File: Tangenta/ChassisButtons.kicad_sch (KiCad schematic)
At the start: 26 parts, among them J2 Conn_02x02_Top_Bottom, Q1 2N7002, Q2 2N7002, SW1 TSC015A04818B, SW2 TSC015A04818B, U7 74HC04D,653, U8 CD4060SA_TR, U9 74HC74D,653

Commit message: Fixes, new approach.
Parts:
- C34, C35, C36, C37, C38, C39: symbol LocalPrjLib:C_Small -> LocalSymbolsPrjLib:C_Small
- J2: symbol LocalPrjLib:Conn_02x02_Top_Bottom -> LocalSymbolsPrjLib:Conn_02x02_Top_Bottom
- Q1, Q2: symbol LocalPrjLib:2N7002 -> LocalSymbolsPrjLib:2N7002
- R15, R16, R17, R18, R19, R20, R21, R22, R23, R24, R25, R26: symbol LocalPrjLib:R_Small_US -> LocalSymbolsPrjLib:R_Small_US
- SW1, SW2: symbol LocalPrjLib:TSC015A04818B -> LocalSymbolsPrjLib:TSC015A04818B
- U7: symbol LocalPrjLib:74HC04D,653 -> LocalSymbolsPrjLib:74HC04D,653
- U8: symbol LocalPrjLib:CD4060SA_TR -> LocalSymbolsPrjLib:CD4060SA_TR
- U9: symbol LocalPrjLib:74HC74D,653 -> LocalSymbolsPrjLib:74HC74D,653
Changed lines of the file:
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@@
     )
   )
-  (symbol (lib_id "LocalPrjLib:R_Small_US") (at 68.58 74.93 0) (unit 1)
+  (symbol (lib_id "LocalSymbolsPrjLib:R_Small_US") (at 68.58 74.93 0) (unit 1)
     (in_bom no) (on_board yes) (dnp yes) (fields_autoplaced)
     (property "Reference" "R16" (at 71.12 73.66 0)
@@
     )
   )
-  (symbol (lib_id "LocalPrjLib:74HC04D,653") (at 141.605 66.04 0) (unit 1)
+  (symbol (lib_id "LocalSymbolsPrjLib:74HC04D,653") (at 141.605 66.04 0) (unit 1)
     (in_bom yes) (on_board yes) (dnp no)
     (property "Reference" "U7" (at 135.255 54.61 0)
@@
     )
   )
-  (symbol (lib_id "LocalPrjLib:R_Small_US") (at 215.265 121.285 90) (unit 1)
+  (symbol (lib_id "LocalSymbolsPrjLib:R_Small_US") (at 215.265 121.285 90) (unit 1)
     (in_bom yes) (on_board yes) (dnp no)
     (property "Reference" "R23" (at 212.725 120.015 90)
@@
     )
   )
-  (symbol (lib_id "LocalPrjLib:C_Small") (at 142.24 82.55 90) (unit 1)
+  (symbol (lib_id "LocalSymbolsPrjLib:C_Small") (at 142.24 82.55 90) (unit 1)
     (in_bom yes) (on_board yes) (dnp no)
     (property "Reference" "C36" (at 139.065 83.82 90)
@@
     )
   )
-  (symbol (lib_id "LocalPrjLib:R_Small_US") (at 168.275 116.205 90) (unit 1)
+  (symbol (lib_id "LocalSymbolsPrjLib:R_Small_US") (at 168.275 116.205 90) (unit 1)
     (in_bom yes) (on_board yes) (dnp no)
     (property "Reference" "R20" (at 165.735 114.935 90)
@@
     )
   )
-  (symbol (lib_id "LocalPrjLib:TSC015A04818B") (at 60.833 111.125 90) (unit 1)
+  (symbol (lib_id "LocalSymbolsPrjLib:TSC015A04818B") (at 60.833 111.125 90) (unit 1)
     (in_bom yes) (on_board yes) (dnp no)
     (property "Reference" "SW1" (at 58.293 107.315 90)
@@
     )
   )
-  (symbol (lib_id "LocalPrjLib:C_Small") (at 215.265 82.55 90) (unit 1)
+  (symbol (lib_id "LocalSymbolsPrjLib:C_Small") (at 215.265 82.55 90) (unit 1)
     (in_bom yes) (on_board yes) (dnp no)
     (property "Reference" "C39" (at 212.09 83.82 90)
@@
     )
   )
-  (symbol (lib_id "LocalPrjLib:74HC74D,653") (at 215.011 66.167 0) (unit 1)
+  (symbol (lib_id "LocalSymbolsPrjLib:74HC74D,653") (at 215.011 66.167 0) (unit 1)
     (in_bom yes) (on_board yes) (dnp no)
     (property "Reference" "U9" (at 208.661 54.737 0)
@@
     )
   )
-  (symbol (lib_id "LocalPrjLib:R_Small_US") (at 103.505 83.82 90) (unit 1)
+  (symbol (lib_id "LocalSymbolsPrjLib:R_Small_US") (at 103.505 83.82 90) (unit 1)
     (in_bom no) (on_board yes) (dnp yes)
     (property "Reference" "R18" (at 102.235 82.55 90)
@@
     )
   )
-  (symbol (lib_id "LocalPrjLib:Conn_02x02_Top_Bottom") (at 76.2 83.82 0) (unit 1)
+  (symbol (lib_id "LocalSymbolsPrjLib:Conn_02x02_Top_Bottom") (at 76.2 83.82 0) (unit 1)
     (in_bom yes) (on_board yes) (dnp no)
     (property "Reference" "J2" (at 77.47 80.645 0)
@@
     )
   )
-  (symbol (lib_id "LocalPrjLib:CD4060SA_TR") (at 141.605 109.855 0) (unit 1)
+  (symbol (lib_id "LocalSymbolsPrjLib:CD4060SA_TR") (at 141.605 109.855 0) (unit 1)
     (in_bom yes) (on_board yes) (dnp no)
     (property "Reference" "U8" (at 135.255 97.155 0)
@@
     )
   )
-  (symbol (lib_id "LocalPrjLib:R_Small_US") (at 237.49 109.855 0) (unit 1)
+  (symbol (lib_id "LocalSymbolsPrjLib:R_Small_US") (at 237.49 109.855 0) (unit 1)
     (in_bom yes) (on_board yes) (dnp no)
     (property "Reference" "R24" (at 238.76 108.585 0)
@@
     )
   )
-  (symbol (lib_id "LocalPrjLib:R_Small_US") (at 86.36 74.93 0) (unit 1)
+  (symbol (lib_id "LocalSymbolsPrjLib:R_Small_US") (at 86.36 74.93 0) (unit 1)
     (in_bom yes) (on_board yes) (dnp no) (fields_autoplaced)
     (property "Reference" "R17" (at 88.9 73.66 0)
@@
     )
   )
-  (symbol (lib_id "LocalPrjLib:C_Small") (at 69.215 111.125 0) (mirror x) (unit 1)
+  (symbol (lib_id "LocalSymbolsPrjLib:C_Small") (at 69.215 111.125 0) (mirror x) (unit 1)
     (in_bom yes) (on_board yes) (dnp no)
     (property "Reference" "C34" (at 70.485 113.665 90)
@@
     )
   )
-  (symbol (lib_id "LocalPrjLib:2N7002") (at 224.155 121.285 0) (unit 1)
+  (symbol (lib_id "LocalSymbolsPrjLib:2N7002") (at 224.155 121.285 0) (unit 1)
     (in_bom yes) (on_board yes) (dnp no)
     (property "Reference" "Q1" (at 227.33 117.475 0)
@@
     )
   )
-  (symbol (lib_id "LocalPrjLib:R_Small_US") (at 211.455 128.905 0) (unit 1)
+  (symbol (lib_id "LocalSymbolsPrjLib:R_Small_US") (at 211.455 128.905 0) (unit 1)
     (in_bom yes) (on_board yes) (dnp no)
     (property "Reference" "R22" (at 212.725 127.635 0)
@@
     )
   )
-  (symbol (lib_id "LocalPrjLib:R_Small_US") (at 252.73 81.28 0) (unit 1)
+  (symbol (lib_id "LocalSymbolsPrjLib:R_Small_US") (at 252.73 81.28 0) (unit 1)
     (in_bom yes) (on_board yes) (dnp no)
     (property "Reference" "R26" (at 254 77.47 90)
@@
     )
   )
-  (symbol (lib_id "LocalPrjLib:R_Small_US") (at 191.135 60.96 270) (unit 1)
+  (symbol (lib_id "LocalSymbolsPrjLib:R_Small_US") (at 191.135 60.96 270) (unit 1)
     (in_bom yes) (on_board yes) (dnp no)
     (property "Reference" "R21" (at 188.595 59.69 90)
@@
     )
   )
-  (symbol (lib_id "LocalPrjLib:R_Small_US") (at 168.275 111.76 90) (unit 1)
+  (symbol (lib_id "LocalSymbolsPrjLib:R_Small_US") (at 168.275 111.76 90) (unit 1)
     (in_bom yes) (on_board yes) (dnp no)
     (property "Reference" "R19" (at 165.735 110.49 90)
@@
     )
   )
-  (symbol (lib_id "LocalPrjLib:R_Small_US") (at 52.07 83.82 90) (unit 1)
+  (symbol (lib_id "LocalSymbolsPrjLib:R_Small_US") (at 52.07 83.82 90) (unit 1)
     (in_bom yes) (on_board yes) (dnp no)
     (property "Reference" "R15" (at 50.8 82.55 90)
@@
     )
   )
-  (symbol (lib_id "LocalPrjLib:R_Small_US") (at 241.3 102.235 90) (unit 1)
+  (symbol (lib_id "LocalSymbolsPrjLib:R_Small_US") (at 241.3 102.235 90) (unit 1)
     (in_bom yes) (on_board yes) (dnp no)
     (property "Reference" "R25" (at 238.76 100.965 90)
@@
     )
   )
-  (symbol (lib_id "LocalPrjLib:TSC015A04818B") (at 87.122 111.125 270) (mirror x) (unit 1)
+  (symbol (lib_id "LocalSymbolsPrjLib:TSC015A04818B") (at 87.122 111.125 270) (mirror x) (unit 1)
     (in_bom yes) (on_board yes) (dnp no)
     (property "Reference" "SW2" (at 89.662 107.315 90)
@@
     )
   )
-  (symbol (lib_id "LocalPrjLib:C_Small") (at 168.275 120.65 90) (unit 1)
+  (symbol (lib_id "LocalSymbolsPrjLib:C_Small") (at 168.275 120.65 90) (unit 1)
     (in_bom yes) (on_board yes) (dnp no)
     (property "Reference" "C38" (at 165.735 119.38 90)
@@
     )
   )
-  (symbol (lib_id "LocalPrjLib:C_Small") (at 78.74 111.125 0) (mirror x) (unit 1)
+  (symbol (lib_id "LocalSymbolsPrjLib:C_Small") (at 78.74 111.125 0) (mirror x) (unit 1)
     (in_bom yes) (on_board yes) (dnp no)
     (property "Reference" "C35" (at 80.01 113.665 90)
@@
     )
   )
-  (symbol (lib_id "LocalPrjLib:2N7002") (at 250.19 102.235 0) (unit 1)
+  (symbol (lib_id "LocalSymbolsPrjLib:2N7002") (at 250.19 102.235 0) (unit 1)
     (in_bom yes) (on_board yes) (dnp no) (fields_autoplaced)
     (property "Reference" "Q2" (at 257.81 100.965 0)
@@
     )
   )
-  (symbol (lib_id "LocalPrjLib:C_Small") (at 142.24 127.635 90) (unit 1)
+  (symbol (lib_id "LocalSymbolsPrjLib:C_Small") (at 142.24 127.635 90) (unit 1)
     (in_bom yes) (on_board yes) (dnp no)
     (property "Reference" "C37" (at 139.065 128.905 90)

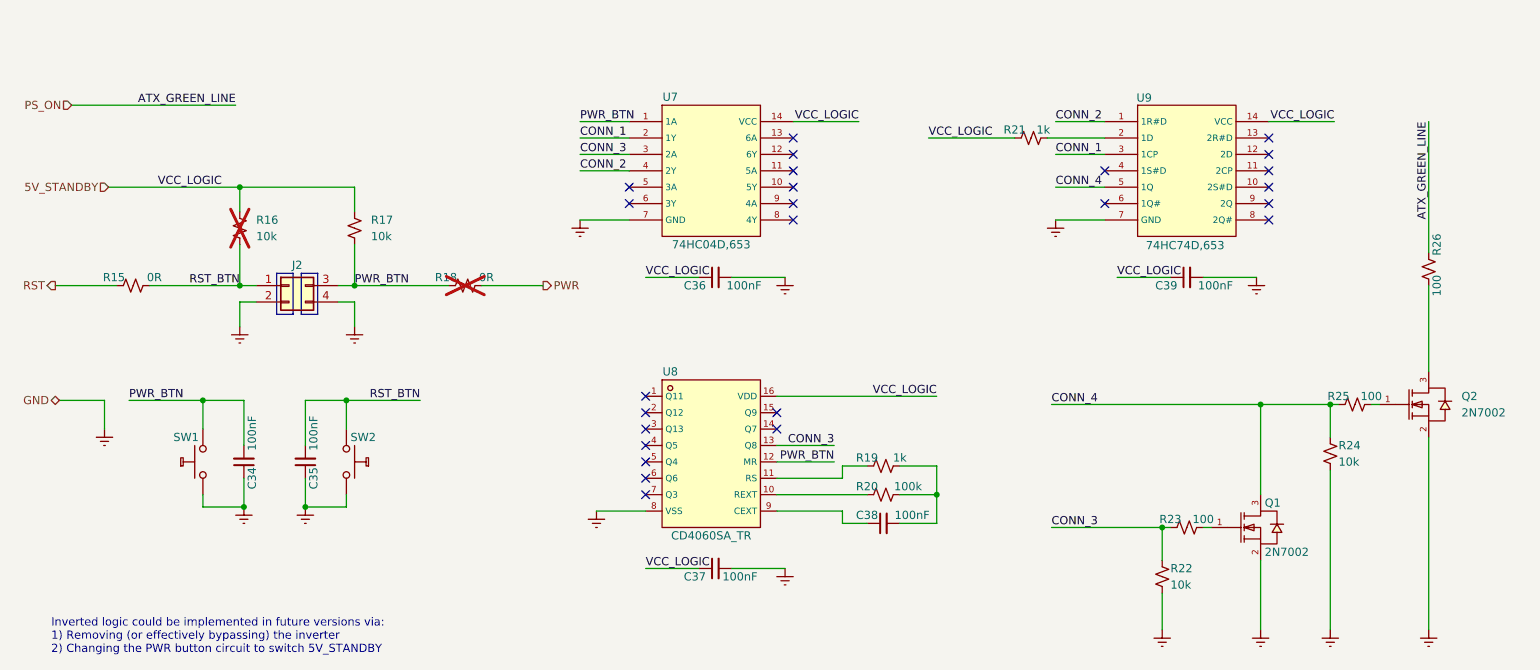
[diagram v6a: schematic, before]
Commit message: Implemented inverted ATX power button (optional).
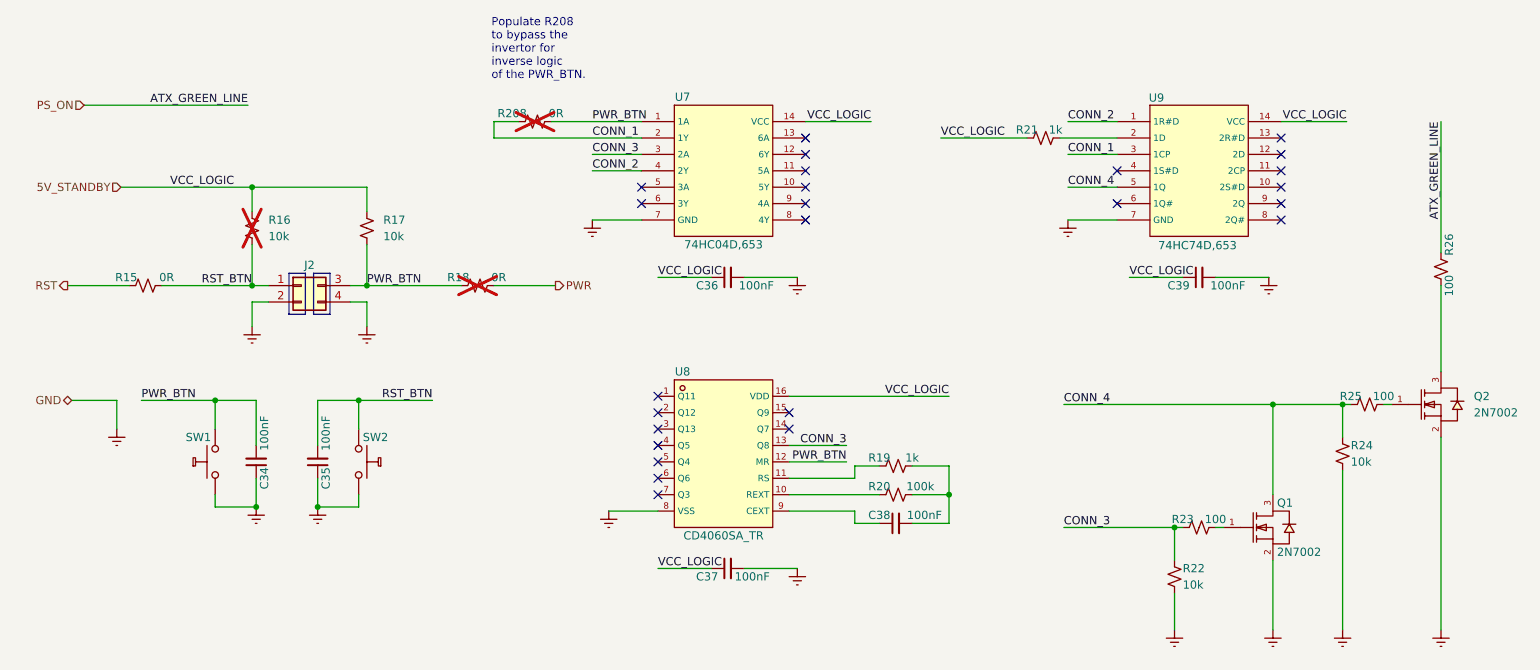
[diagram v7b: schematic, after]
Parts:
- added R208: 0R, Resistor_SMD:R_0603_1608Metric, symbol LocalSymbolsPrjLib:R_Small_US
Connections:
- net CONN_1: now also R208.1
- net PWR_BTN: now also R208.2
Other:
- note added: "Populate R208 to bypass the invertor for inverse logic of the PWR_BTN."
- note removed: "Inverted logic could be implemented in future versions via: 1) Removing (or effectively bypassing) the inverter 2) Changing the PWR button circuit to switch 5V_STANDBY"
- moved on the sheet: C34, C35, C36, C37, C38, C39, J2, Q1, Q2, R15, R16, R17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
